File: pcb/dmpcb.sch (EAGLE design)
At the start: 29 parts, among them IC1 7805DT, IC2 L293D, Q1 IRF530, Q2 IRF530

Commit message: cleanup, nothing else
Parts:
- added J3: GREEN-2P-3.5, Seeed-Connector:SCREW-TERMINAL-GREEN(2P-3.5)
- added R10: (no value), rcl:R-EU_M0805
- added R9: (no value), rcl:R-TRIMM64Y
- added S1: 2P2T, switch:2P2T
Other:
- note added: "Sensorport"
- note added: "Sensorport mit variablem pull up/pull down mit jumper oder schiebeschalter mit trimmer und kleinem widerstand 7 Segment mit shiftregister Dotmatrix?"
- note added: "jumper am 7805 vorbei"
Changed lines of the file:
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@@
 <layer number="154" name="FabDoc2" color="2" fill="1" visible="no" active="no"/>
 <layer number="155" name="FabDoc3" color="7" fill="15" visible="no" active="no"/>
+<layer number="166" name="AntennaArea" color="7" fill="1" visible="yes" active="yes"/>
+<layer number="168" name="4mmHeightArea" color="7" fill="1" visible="yes" active="yes"/>
 <layer number="199" name="Contour" color="7" fill="1" visible="no" active="no"/>
 <layer number="200" name="200bmp" color="1" fill="10" visible="no" active="no"/>
@@
 <part name="GND13" library="supply1" library_urn="urn:adsk.eagle:library:371" deviceset="GND" device=""/>
 <part name="C4" library="rcl" library_urn="urn:adsk.eagle:library:334" deviceset="C-EU" device="C0805" package3d_urn="urn:adsk.eagle:package:23617/2" value="100uf"/>
+<part name="J3" library="Seeed-Connector" library_urn="urn:adsk.eagle:library:478" deviceset="SCREW-TERMINAL-GREEN(2P-3.5)" device="" package3d_urn="urn:adsk.eagle:package:33118/1" value="GREEN-2P-3.5"/>
+<part name="R9" library="rcl" library_urn="urn:adsk.eagle:library:334" deviceset="R-TRIMM" device="64Y" package3d_urn="urn:adsk.eagle:package:23750/1"/>
+<part name="R10" library="rcl" library_urn="urn:adsk.eagle:library:334" deviceset="R-EU_" device="M0805" package3d_urn="urn:adsk.eagle:package:23556/1"/>
+<part name="S1" library="switch" library_urn="urn:adsk.eagle:library:380" deviceset="2P2T" device="" package3d_urn="urn:adsk.eagle:package:27753/1"/>
 </parts>
 <sheets>
@@
 <text x="152.4" y="129.54" size="6.4516" layer="91">POTS</text>
 <text x="317.5" y="129.54" size="6.4516" layer="91">STEPPERDRIVER</text>
+<text x="109.22" y="187.96" size="1.778" layer="91">jumper am 7805 vorbei</text>
+<text x="241.3" y="50.8" size="1.778" layer="91">Sensorport
+mit variablem pull up/pull down mit jumper oder schiebeschalter mit trimmer und kleinem widerstand
+7 Segment mit shiftregister
+Dotmatrix?</text>
+<text x="152.4" y="55.88" size="6.4516" layer="91">Sensorport</text>
 </plain>
 <instances>
@@
 <instance part="C4" gate="G$1" x="347.98" y="93.98" smashed="yes">
 <attribute name="NAME" x="341.884" y="91.821" size="1.778" layer="95"/>
-<attribute name="VALUE" x="341.884" y="89.281" size="1.778" layer="96"/>
+</instance>
+<instance part="J3" gate="G$1" x="220.98" y="35.56" smashed="yes">
+<attribute name="NAME" x="214.63" y="41.91" size="1.27" layer="95" ratio="10"/>
+<attribute name="VALUE" x="220.98" y="41.91" size="1.27" layer="96" ratio="10"/>
+</instance>
+<instance part="R9" gate="G$1" x="193.04" y="38.1" smashed="yes">
+<attribute name="NAME" x="187.071" y="34.29" size="1.778" layer="95" rot="R90"/>
+<attribute name="VALUE" x="189.23" y="34.29" size="1.778" layer="96" rot="R90"/>
+</instance>
+<instance part="R10" gate="G$1" x="205.74" y="38.1" smashed="yes">
+<attribute name="NAME" x="201.93" y="39.5986" size="1.778" layer="95"/>
+<attribute name="VALUE" x="201.93" y="34.798" size="1.778" layer="96"/>
+</instance>
+<instance part="S1" gate="G$1" x="177.8" y="38.1" smashed="yes" rot="R90">
+<attribute name="NAME" x="176.53" y="43.18" size="1.778" layer="95" rot="R90"/>
+<attribute name="VALUE" x="179.07" y="43.18" size="1.778" layer="96" rot="R90"/>
 </instance>
 </instances>
@@
 <wire x1="236.22" y1="68.58" x2="152.4" y2="68.58" width="0.1524" layer="91"/>
 <wire x1="152.4" y1="68.58" x2="152.4" y2="139.7" width="0.1524" layer="91"/>
+<wire x1="152.4" y1="68.58" x2="152.4" y2="139.7" width="0.1524" layer="91"/>
 </segment>
 </net>
@@
 </segment>
 </net>
+<net name="N$15" class="0">
+<segment>
+<wire x1="152.4" y1="63.5" x2="152.4" y2="-2.54" width="0.1524" layer="91"/>
+<wire x1="152.4" y1="-2.54" x2="236.22" y2="-2.54" width="0.1524" layer="91"/>
+<wire x1="236.22" y1="-2.54" x2="236.22" y2="66.04" width="0.1524" layer="91"/>
+<wire x1="236.22" y1="66.04" x2="152.4" y2="66.04" width="0.1524" layer="91"/>
+<wire x1="152.4" y1="66.04" x2="152.4" y2="63.5" width="0.1524" layer="91"/>
+</segment>
+</net>

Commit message: added Todo to file, buttons, sensorport with variable resistors (had the idea of maybe enabling one of the potis to be jumpered in as a variable resistor?) and 12v to lm293
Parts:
- removed DCMOTORVCC: (no value), SparkFun-Connectors:CONN_022.54MM_SCREWTERM
- removed J3: GREEN-2P-3.5, Seeed-Connector:SCREW-TERMINAL-GREEN(2P-3.5)
- removed S1: 2P2T, switch:2P2T
- added JP3: (no value), jumper:JP3Q
- added R11: 10K, rcl:R-EU_M0805
- added R12, R13: 10k, rcl:R-EU_M0805
- added SENSOR: (no value), SparkFun-Connectors:CONN_022.54MM_SCREWTERM
- R10: value (none) -> 10M
- R7, R8: value (none) -> b10k
- R9: value (none) -> 1M; device rcl:R-TRIMM64Y -> rcl:R-EU_M0805
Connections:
- removed net N$4: DCMOTORVCC.1, IC2.VCC2
- new net BUTTON1: R12.2, U$1.D5
- new net BUTTON2: R13.2, U$1.D7
- new net N$16: JP3.5, R10.1
- new net N$17: JP3.3, R9.1
- new net N$18: JP3.1, R11.1
- new net N$20: R10.2, R11.2, R9.2, SENSOR.1
- new net SENSORPORT: JP3.2, JP3.4, JP3.6, U$1.D29/A18
- net GND: now also R12.1, R13.1, SENSOR.2; no longer DCMOTORVCC.2
- net V+: now also IC2.VCC2
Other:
- note added: "BUTTONS"
- note added: "SENSORPORT"
- note added: "TODO Sensorport mit variablem pull up/pull down mit jumper oder schiebeschalter mit trimmer und kleinem widerstand -> Done 7 Segment mit shiftregister Dotmatrix? Anschlüsse gejumpert, wenn was anderes angesclossen werden soll, jumper ziehen Potis b10k -> done Buttons -> done Farbcode für jumper LM293 Strom von 12v in -> done Opamp-Verstärker"
- note added: "button here"
- note removed: "Sensorport"
- note removed: "Sensorport mit variablem pull up/pull down mit jumper oder schiebeschalter mit trimmer und kleinem widerstand 7 Segment mit shiftregister Dotmatrix?"

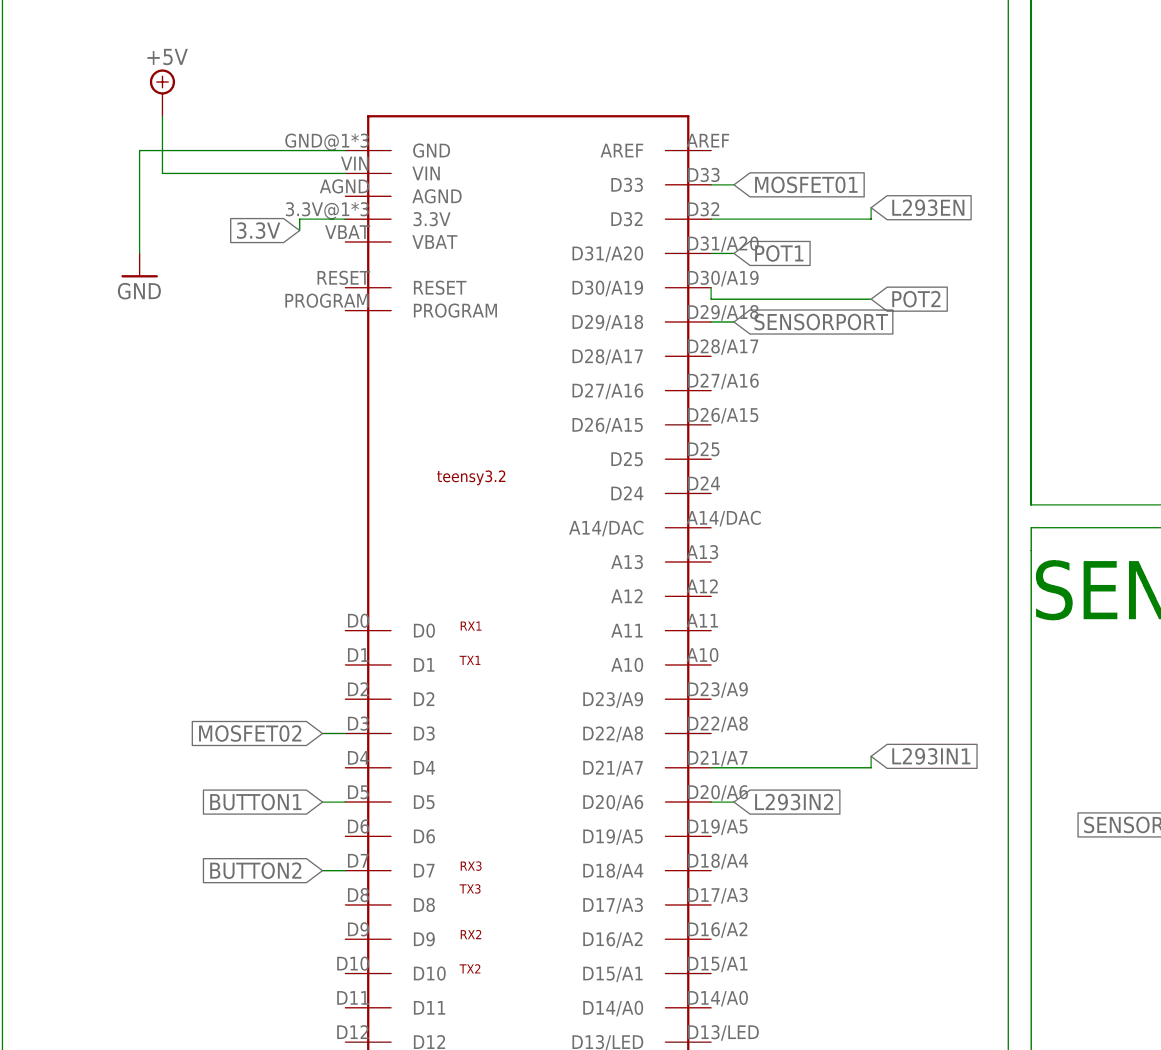
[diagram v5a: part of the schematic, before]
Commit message: changed portlayout, added DNC to the pins in the middle of the teensy
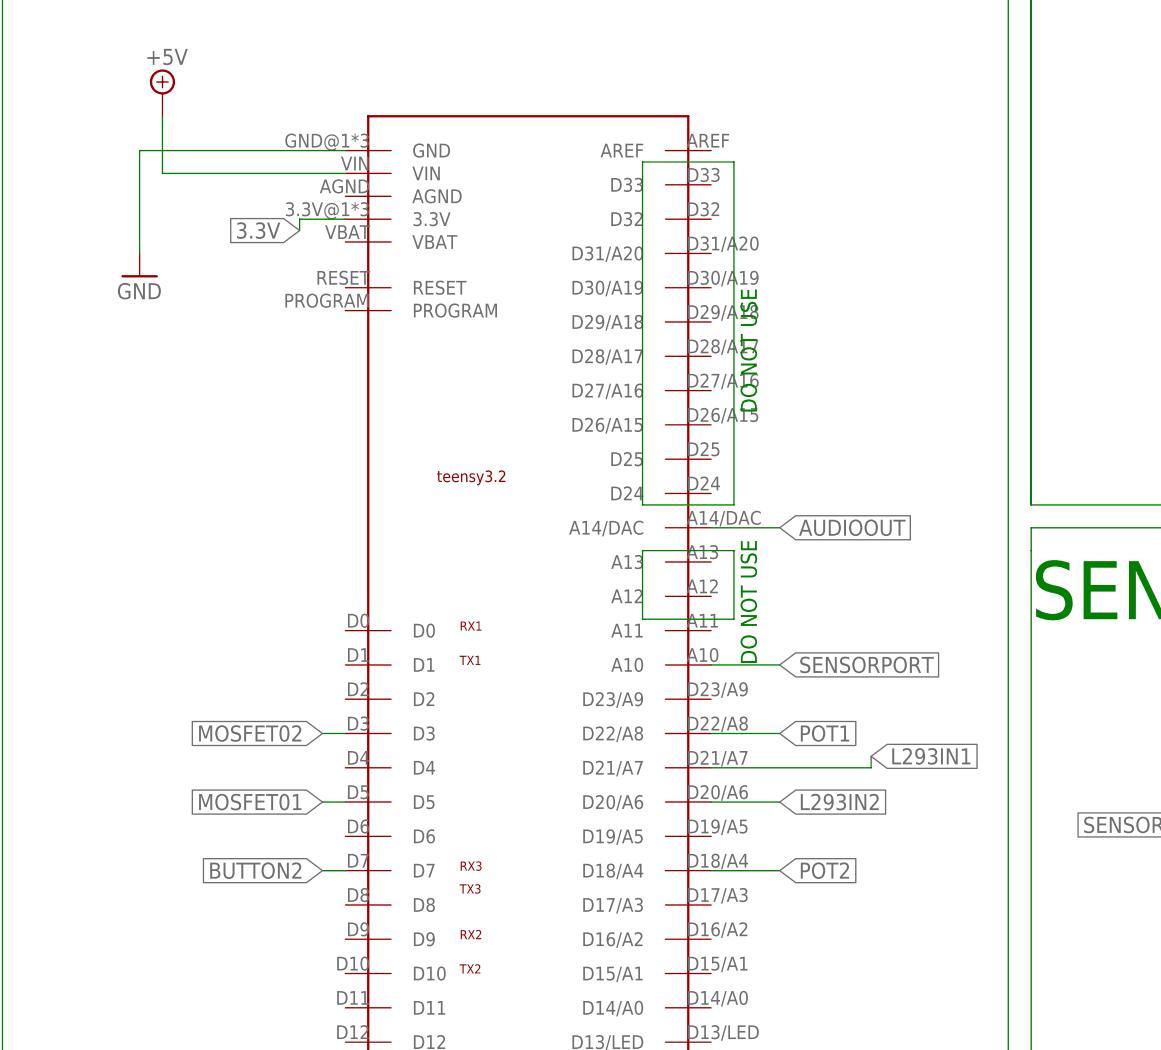
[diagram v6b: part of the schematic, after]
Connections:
- new net AUDIOOUT: U$1.A14/DAC
- net BUTTON1: no longer U$1.D5
- net L293EN: no longer U$1.D32
- net MOSFET01: now also U$1.D5; no longer U$1.D33
- net POT1: now also U$1.D22/A8; no longer U$1.D31/A20
- net POT2: now also U$1.D18/A4; no longer U$1.D30/A19
- net SENSORPORT: now also U$1.A10; no longer U$1.D29/A18
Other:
- note added: "DO NOT USE"
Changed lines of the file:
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@@
 <text x="261.62" y="35.56" size="1.778" layer="91">button here</text>
 <text x="289.56" y="35.56" size="1.778" layer="91">button here</text>
+<text x="121.92" y="78.74" size="1.778" layer="91" rot="R90">DO NOT USE</text>
+<text x="121.92" y="50.8" size="1.778" layer="91" rot="R90">DO NOT USE</text>
 </plain>
 <instances>
@@
 <net name="L293EN" class="0">
 <segment>
-<pinref part="U$1" gate="G$1" pin="D32"/>
-<wire x1="116.84" y1="100.33" x2="134.62" y2="100.33" width="0.1524" layer="91"/>
-<wire x1="134.62" y1="100.33" x2="134.62" y2="101.6" width="0.1524" layer="91"/>
-<label x="134.62" y="101.6" size="1.778" layer="95" xref="yes"/>
-</segment>
-<segment>
 <pinref part="IC2" gate="G$1" pin="1-2EN"/>
 <wire x1="347.98" y1="198.12" x2="345.44" y2="198.12" width="0.1524" layer="91"/>
@@
 <segment>
 <pinref part="U$1" gate="G$1" pin="D20/A6"/>
-<wire x1="116.84" y1="35.56" x2="119.38" y2="35.56" width="0.1524" layer="91"/>
-<label x="119.38" y="35.56" size="1.778" layer="95" xref="yes"/>
+<wire x1="116.84" y1="35.56" x2="124.46" y2="35.56" width="0.1524" layer="91"/>
+<label x="124.46" y="35.56" size="1.778" layer="95" xref="yes"/>
 </segment>
 </net>
@@
 </segment>
 <segment>
-<pinref part="U$1" gate="G$1" pin="D33"/>
-<wire x1="116.84" y1="104.14" x2="119.38" y2="104.14" width="0.1524" layer="91"/>
-<label x="119.38" y="104.14" size="1.778" layer="95" xref="yes"/>
+<pinref part="U$1" gate="G$1" pin="D5"/>
+<wire x1="76.2" y1="35.56" x2="73.66" y2="35.56" width="0.1524" layer="91"/>
+<label x="73.66" y="35.56" size="1.778" layer="95" rot="R180" xref="yes"/>
 </segment>
 </net>
@@
 </segment>
 <segment>
-<pinref part="U$1" gate="G$1" pin="D31/A20"/>
-<wire x1="116.84" y1="96.52" x2="119.38" y2="96.52" width="0.1524" layer="91"/>
-<label x="119.38" y="96.52" size="1.778" layer="95" xref="yes"/>
+<pinref part="U$1" gate="G$1" pin="D22/A8"/>
+<wire x1="116.84" y1="43.18" x2="124.46" y2="43.18" width="0.1524" layer="91"/>
+<label x="124.46" y="43.18" size="1.778" layer="95" xref="yes"/>
 </segment>
 </net>
@@
 </segment>
 <segment>
-<pinref part="U$1" gate="G$1" pin="D30/A19"/>
-<wire x1="116.84" y1="92.71" x2="116.84" y2="91.44" width="0.1524" layer="91"/>
-<wire x1="116.84" y1="91.44" x2="134.62" y2="91.44" width="0.1524" layer="91"/>
-<label x="134.62" y="91.44" size="1.778" layer="95" xref="yes"/>
+<pinref part="U$1" gate="G$1" pin="D18/A4"/>
+<wire x1="116.84" y1="27.94" x2="124.46" y2="27.94" width="0.1524" layer="91"/>
+<label x="124.46" y="27.94" size="1.778" layer="95" xref="yes"/>
 </segment>
 </net>
@@
 <net name="SENSORPORT" class="0">
 <segment>
-<pinref part="U$1" gate="G$1" pin="D29/A18"/>
-<wire x1="116.84" y1="88.9" x2="119.38" y2="88.9" width="0.1524" layer="91"/>
-<label x="119.38" y="88.9" size="1.778" layer="95" xref="yes"/>
-</segment>
-<segment>
 <pinref part="JP3" gate="B" pin="2"/>
 <pinref part="JP3" gate="B" pin="4"/>
@@
 <label x="175.26" y="33.02" size="1.778" layer="95" rot="R180" xref="yes"/>
 </segment>
+<segment>
+<pinref part="U$1" gate="G$1" pin="A10"/>
+<wire x1="116.84" y1="50.8" x2="124.46" y2="50.8" width="0.1524" layer="91"/>
+<label x="124.46" y="50.8" size="1.778" layer="95" xref="yes"/>
+</segment>
 </net>
 <net name="N$4" class="0">
@@
 <net name="BUTTON1" class="0">
 <segment>
-<pinref part="U$1" gate="G$1" pin="D5"/>
-<wire x1="76.2" y1="35.56" x2="73.66" y2="35.56" width="0.1524" layer="91"/>
-<label x="73.66" y="35.56" size="1.778" layer="95" rot="R180" xref="yes"/>
-</segment>
-<segment>
 <pinref part="R12" gate="G$1" pin="2"/>
 <wire x1="261.62" y1="30.48" x2="261.62" y2="27.94" width="0.1524" layer="91"/>
@@
 </segment>
 </net>
+<net name="N$22" class="0">
+<segment>
+<wire x1="119.38" y1="55.88" x2="109.22" y2="55.88" width="0.1524" layer="91"/>
+<wire x1="109.22" y1="55.88" x2="109.22" y2="63.5" width="0.1524" layer="91"/>
+<wire x1="109.22" y1="63.5" x2="119.38" y2="63.5" width="0.1524" layer="91"/>
+<wire x1="119.38" y1="63.5" x2="119.38" y2="55.88" width="0.1524" layer="91"/>
+</segment>
+</net>
+<net name="N$23" class="0">
+<segment>
+<wire x1="119.38" y1="68.58" x2="109.22" y2="68.58" width="0.1524" layer="91"/>
+<wire x1="109.22" y1="68.58" x2="109.22" y2="106.68" width="0.1524" layer="91"/>
+<wire x1="109.22" y1="106.68" x2="119.38" y2="106.68" width="0.1524" layer="91"/>
+<wire x1="119.38" y1="106.68" x2="119.38" y2="68.58" width="0.1524" layer="91"/>
+</segment>
+</net>
+<net name="AUDIOOUT" class="0">
+<segment>
+<pinref part="U$1" gate="G$1" pin="A14/DAC"/>
+<wire x1="116.84" y1="66.04" x2="124.46" y2="66.04" width="0.1524" layer="91"/>
+<label x="124.46" y="66.04" size="1.778" layer="95" xref="yes"/>
+</segment>
+</net>

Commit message: changed some parts around, added max7219 (only needed if we chose discrete implementation, not the readymade board -> because more expensive), changed the pins around on the teensy. The stepperdriver still needs to be connected. what about a second motor for the hbridge?
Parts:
- removed C4: 100uf, rcl:C-EUC0805
- added C5: 100nf, rcl:C-EUC0805
- added C6: 10uf, rcl:CPOL-EUB
- added C7: 100uf, rcl:CPOL-EUD
- added IC3: MAX7219CNG, maxim:MAX7219CNG
- added R14: 10k, rcl:R-EU_M0805
- added S1, S2: (no value), switch-omron:10-XX
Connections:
- removed net BUTTON1: R12.2
- removed net BUTTON2: R13.2, U$1.D7
- removed net L293IN1: IC2.1A, U$1.D21/A7
- removed net L293IN2: IC2.2A, U$1.D20/A6
- new net BUTTON01: R12.2, S1.P, S1.P1, U$1.D4
- new net BUTTON02: R13.2, S2.P, S2.P1, U$1.D5
- new net L293IN01: IC2.1A, U$1.D6
- new net L293IN02: IC2.2A, U$1.D7
- new net MAX7219CLK: IC3.CLK, U$1.D12
- new net MAX7219DIN: IC3.DIN, U$1.D10
- new net MAX7219LOAD: IC3.LOAD, U$1.D11
- new net N$19: S1.S, S1.S1
- new net N$21: S2.S, S2.S1
- new net N$25: IC3.ISET, R14.1
- new net N$29: U$1.D0
- new net N$32: U$1.D23/A9
- new net N$33: U$1.D21/A7
- new net N$34: U$1.D19/A5
- new net N$35: U$1.D20/A6
- new net POT01: R7.3, U$1.A11
- new net POT02: R8.3, U$1.A10
- net +5V: now also C5.1, C6.+, IC3.VCC, R14.2
- net GND: now also C5.2, C6.-, C7.-, IC3.GND@1, IC3.GND@2; no longer C4.1
- net L293EN: now also U$1.D8
- net MOSFET01: now also U$1.D2; no longer U$1.D5
- net POT1: no longer R7.3
- net POT2: no longer R8.3
- net SENSORPORT: now also U$1.D9; no longer U$1.A10
- net VMOT: now also C7.+; no longer C4.2
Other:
- note added: "MAX7219"
- note added: "TODO Sensorport mit variablem pull up/pull down mit jumper oder schiebeschalter mit trimmer und kleinem widerstand -> Done Dotmatrix mit max7219 Anschlüsse gejumpert, wenn was anderes angesclossen werden soll, jumper ziehen Potis b10k -> done Buttons -> done Farbcode für jumper LM293 Strom von 12v in -> done Opamp-Verstärker"
- note added: "pwm?"
- note removed: "TODO Sensorport mit variablem pull up/pull down mit jumper oder schiebeschalter mit trimmer und kleinem widerstand -> Done 7 Segment mit shiftregister Dotmatrix? Anschlüsse gejumpert, wenn was anderes angesclossen werden soll, jumper ziehen Potis b10k -> done Buttons -> done Farbcode für jumper LM293 Strom von 12v in -> done Opamp-Verstärker"
- note removed: "button here"

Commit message: found footprint for drv8825 carrier board, included it into schematic
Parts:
- added J3, J4: (no value), SparkFun-Connectors:CONN_18
- added U$2: POLOLU-DRV8825, alvarop-lib:POLOLU-DRV8825
- J1, J2: device SparkFun-Connectors:CONN_08" -> SparkFun-Connectors:CONN_18
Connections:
- removed net COIL1A: J2.4
- removed net COIL1B: J2.5
- removed net COIL2A: J2.3
- removed net COIL2B: J2.6
- new net A1: U$2.A1
- new net A2: U$2.A2
- new net B1: U$2.B1
- new net B2: U$2.B2
- net DIR: now also U$2.DIR; no longer J1.8
- net DNC: now also U$2.FLT_N; no longer J2.2
- net EN: now also U$2.EN_N; no longer J1.1
- net GND: now also U$2.GND, U$2.GND2; no longer J2.1, J2.7
- net M0: now also U$2.M0; no longer J1.2
- net M1: now also U$2.M1; no longer J1.3
- net M2: now also U$2.M2; no longer J1.4
- net RST: now also U$2.RST_N; no longer J1.5
- net SLP: now also U$2.SLP_N; no longer J1.6
- net STP: now also U$2.STEP; no longer J1.7
- net VMOT: now also U$2.VMOT; no longer J2.8
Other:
- moved on the sheet: C7
